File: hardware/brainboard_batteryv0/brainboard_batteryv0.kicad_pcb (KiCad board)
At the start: 2 copper layers, 86.4 x 54.6 mm, 62 parts, among them CON1 USB-MINI-B, P1 JST, P10 3V3, P2 VBAT, P3 GND, P4 BBB_PMIC, P5 ~ALRT, P6 VBUS, P7 WP, P8 EN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

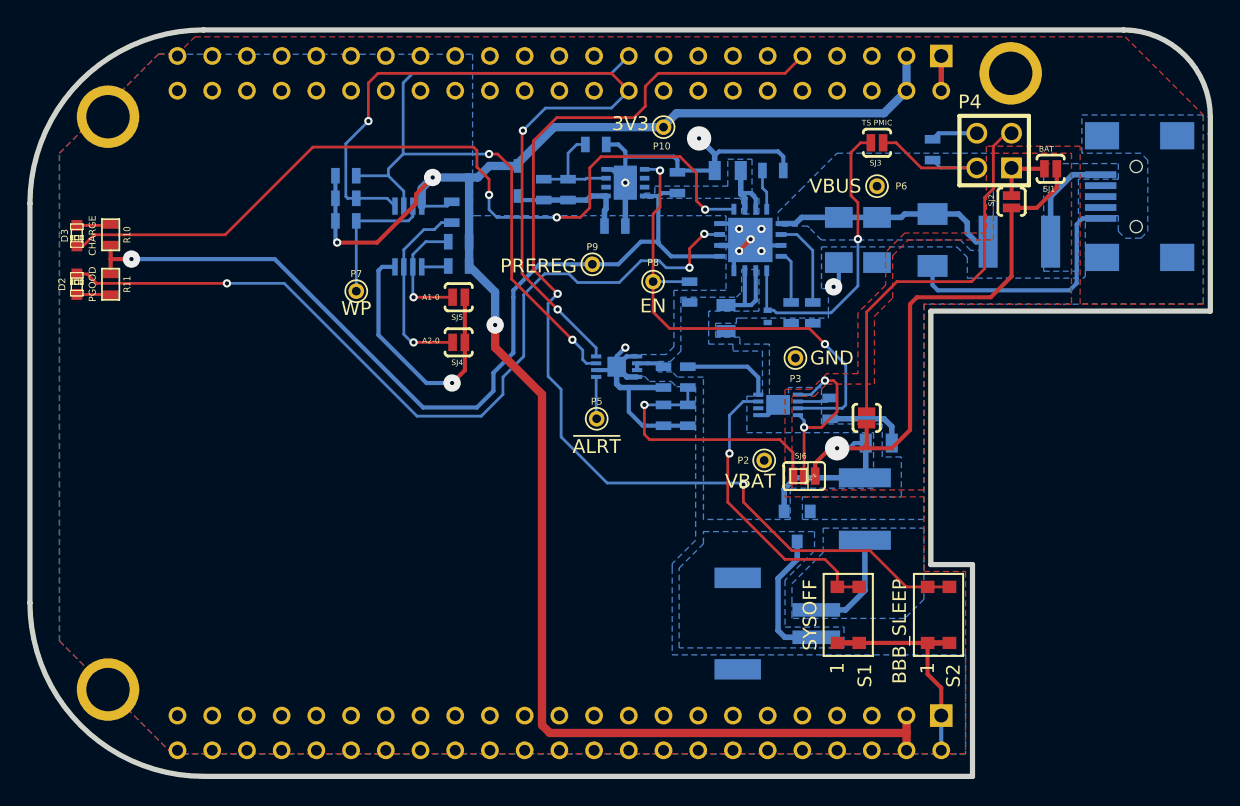
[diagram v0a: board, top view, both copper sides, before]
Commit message: Finalized hole positions, gerbers/drills
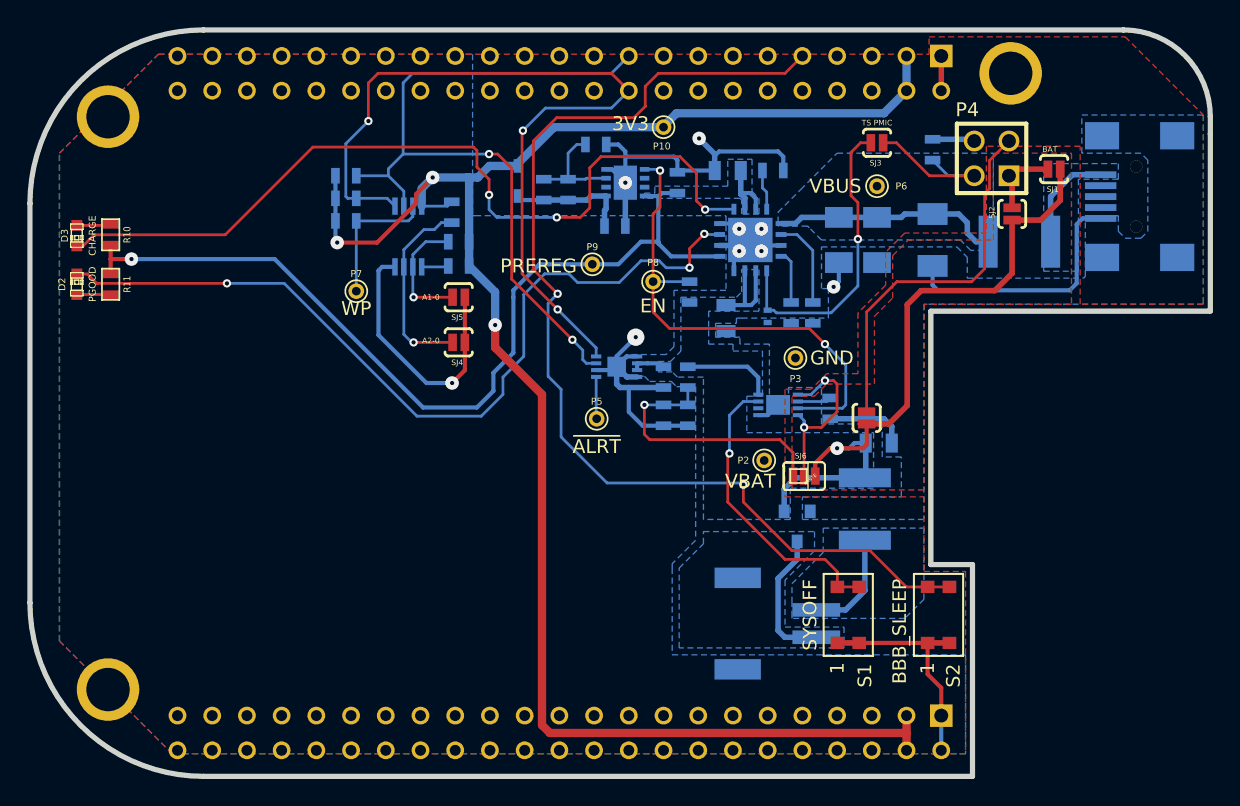
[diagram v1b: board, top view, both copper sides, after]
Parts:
- F2: value PTC 1.95A -> 1.95A
- moved SJ2 0.89 mm to (255.0, 123.1)
- moved P4 0.60 mm to (253.5, 119.0)
- moved SJ1 0.26 mm to (258.1, 119.8)
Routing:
- net +BATT: track 67.9 -> 66.0 mm
- net GND: track 127.3 -> 125.7 mm, vias 10 -> 9
- net /BAT: track 4.46 -> 5.49 mm
- net /SENSE: track 28.2 -> 27.3 mm
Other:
- net class High Current: via_dia 1.778 -> 0.9906; via_drill 1.27 -> 0.635
